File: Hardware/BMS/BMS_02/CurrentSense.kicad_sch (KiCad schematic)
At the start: 23 parts, among them U10 OPA320-Q1, U24 INA181, U25 INA181

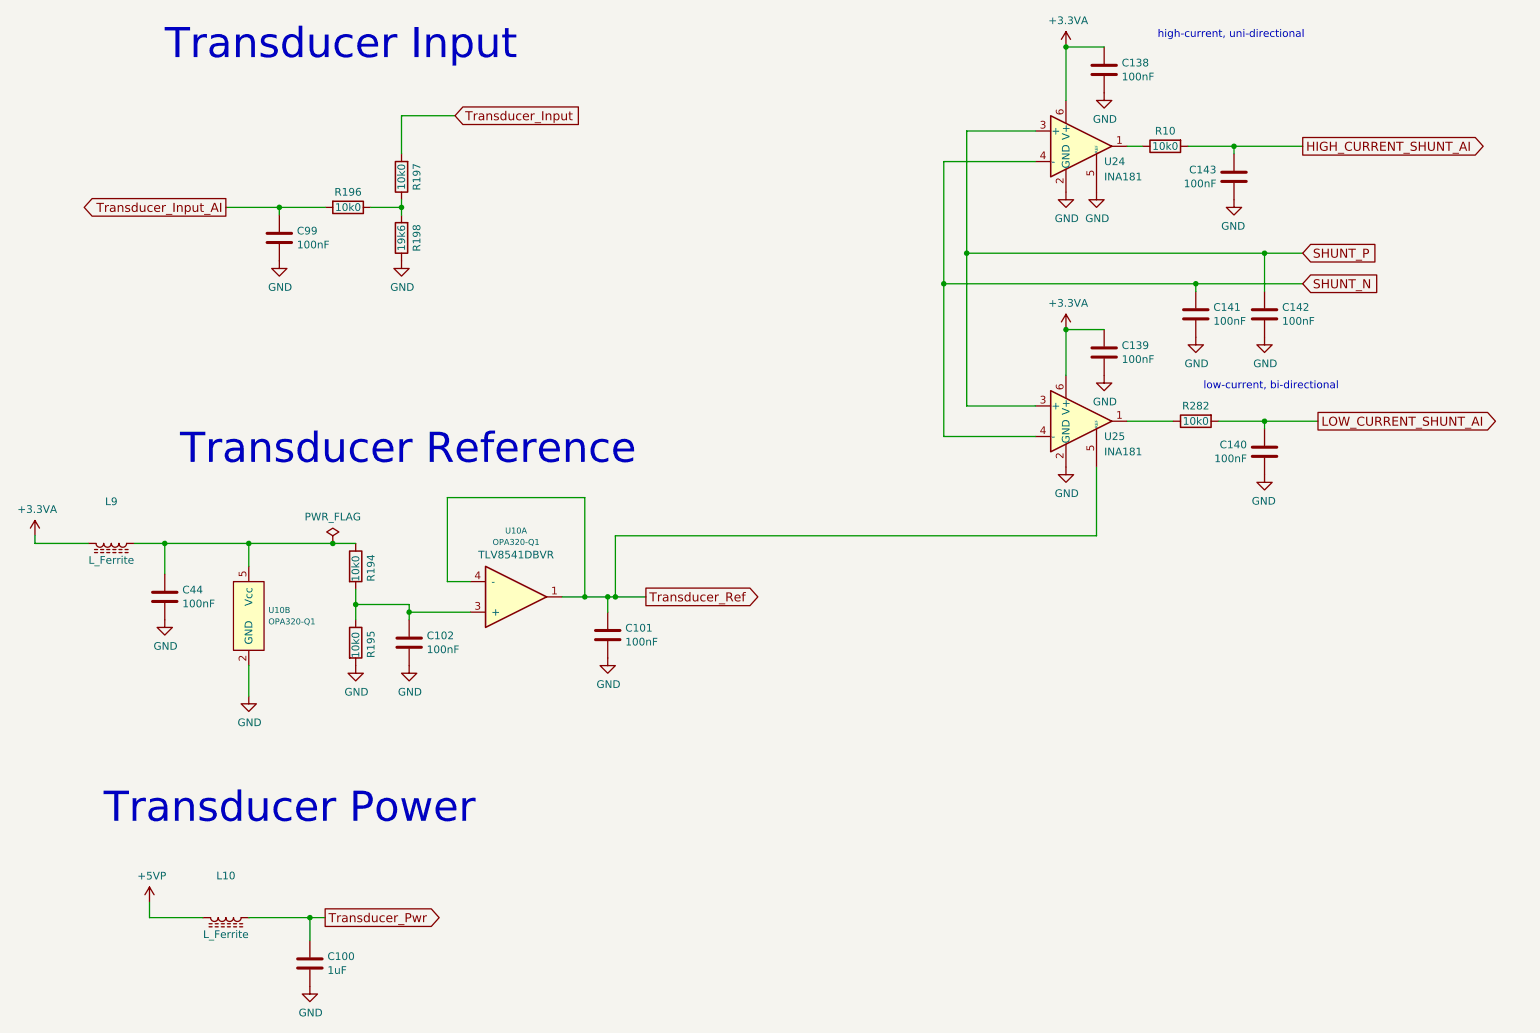
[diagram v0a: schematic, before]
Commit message: bms 02 build and code bring up. Board is built, bootloader is stable and uploads app flawlessly.
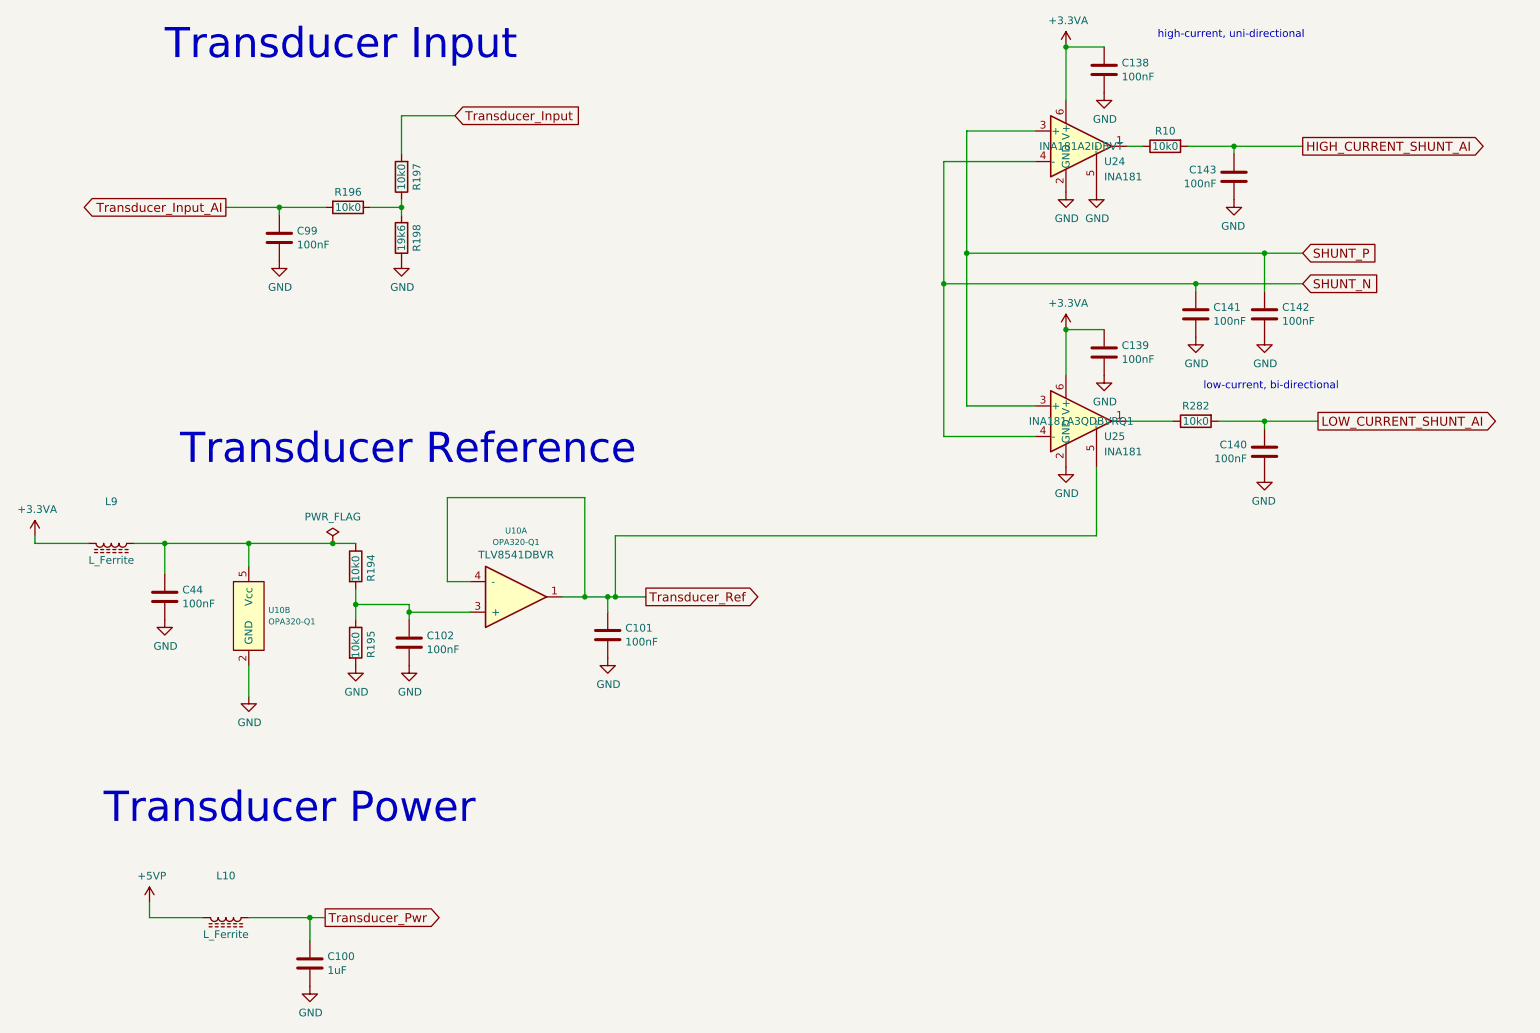
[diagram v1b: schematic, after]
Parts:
- C101, C102, C138, C139, C140, C141, C142, C143, C44, C99, R10, R194, R195, R196, R197, R282: DNP < ... > -> (none)
- U24: MPN (none) -> INA181A2IDBVT
- U25: MPN (none) -> INA181A3QDBVRQ1
